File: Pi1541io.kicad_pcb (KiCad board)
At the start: 2 copper layers, 65 x 56 mm, 22 parts, among them J1 IEC1, J2 IEC2, J3 IEC3, J4 ExtSpkr, P1 Conn_02x20_Odd_Even, SW1 SW_Push, SW2 SW_Push, SW3 SW_Push, SW4 SW_Push, SW5 SW_Push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

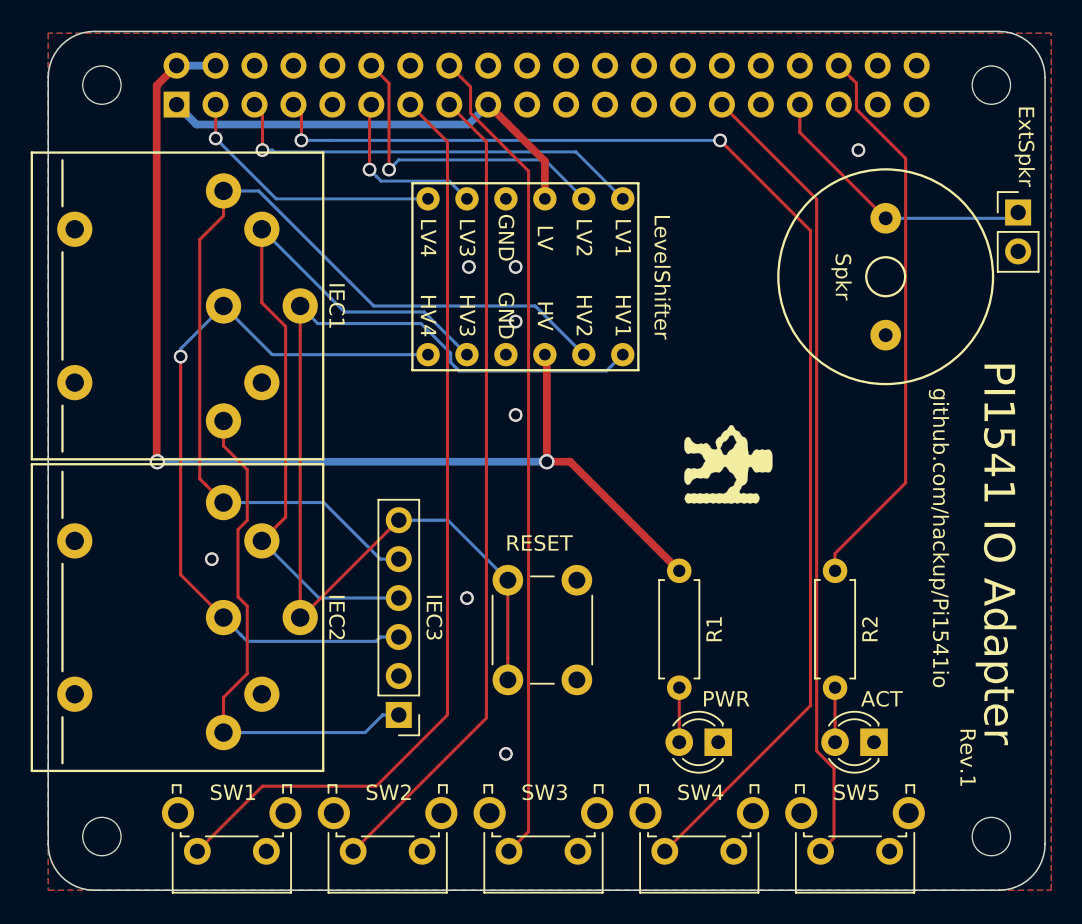
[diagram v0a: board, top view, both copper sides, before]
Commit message: Adding alternate TXS0108 level shifter module to choose from.
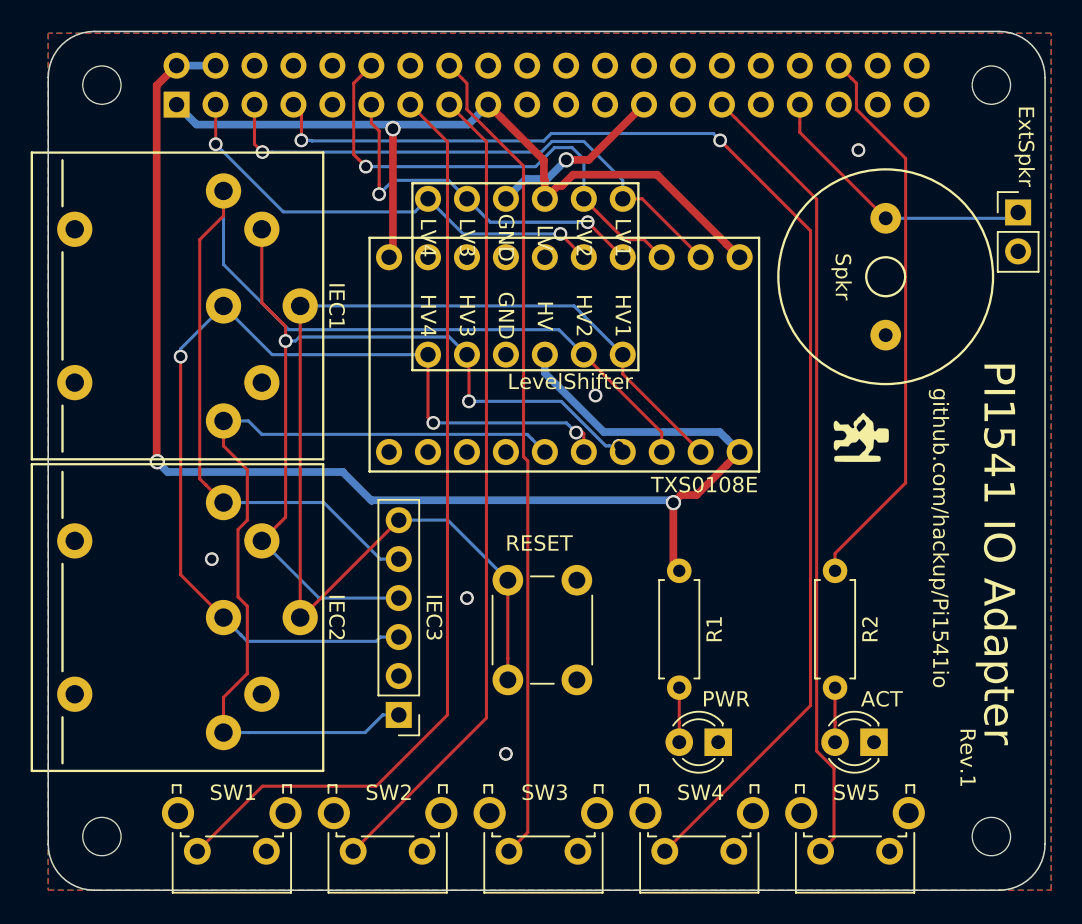
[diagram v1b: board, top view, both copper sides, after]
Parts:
- removed the G*** at (150.6, 87.5)
- added G***: LOGO, Logo:bigby2, F.Cu at (159.2, 85.7)
- added U2: TXS0108E, hackup:TXS0108Module, F.Cu at (138.5, 80.3)
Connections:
- net Net-(J1-Pad1) renamed SRQ
- J1 pad 3: Net-(J1-Pad3) -> ATN
- J1 pad 4: Net-(J1-Pad4) -> CLK
- J1 pad 5: Net-(J1-Pad5) -> DATA
- J1 pad 6: Net-(J1-Pad6) -> RESET
- J2 pad 3: Net-(J1-Pad3) -> ATN
- J2 pad 4: Net-(J1-Pad4) -> CLK
- J2 pad 5: Net-(J1-Pad5) -> DATA
- J2 pad 6: Net-(J1-Pad6) -> RESET
- J3 pad 3: Net-(J1-Pad3) -> ATN
- J3 pad 4: Net-(J1-Pad4) -> CLK
- J3 pad 5: Net-(J1-Pad5) -> DATA
- J3 pad 6: Net-(J1-Pad6) -> RESET
- P1 pad 11: CLK -> CLK_3V
- P1 pad 12: DATA -> DATA_3V
- P1 pad 3: ATN -> ATN_3V
- P1 pad 5: RESET -> RESET_3V
- SW6 pad 1: Net-(J1-Pad6) -> RESET
- U1 pad 1: RESET -> RESET_3V
- U1 pad 11: Net-(J1-Pad5) -> DATA
- U1 pad 12: Net-(J1-Pad6) -> RESET
- U1 pad 2: DATA -> DATA_3V
- U1 pad 5: CLK -> CLK_3V
- U1 pad 6: ATN -> ATN_3V
- U1 pad 7: Net-(J1-Pad3) -> ATN
- U1 pad 8: Net-(J1-Pad4) -> CLK
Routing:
- net Net-(J1-Pad6): track 68.2 -> 0.00 mm
- net Net-(J1-Pad5): track 62.5 -> 0.00 mm
- net DATA: track 21.3 -> 73.7 mm, vias 1 -> 0
- net Net-(J1-Pad3): track 49.5 -> 0.00 mm, vias 1 -> 0
- net Net-(J1-Pad4): track 48.8 -> 0.00 mm
- net CLK: track 11.4 -> 59.2 mm, vias 1 -> 3
- net ATN: track 17.7 -> 65.4 mm, vias 1 -> 3
- net RESET: track 28.0 -> 75.4 mm, vias 1 -> 0
- net RESET_3V: track 0.00 -> 36.0 mm, vias 0 -> 1
- net DATA_3V: track 0.00 -> 31.7 mm, vias 0 -> 1
- net ATN_3V: track 0.00 -> 30.4 mm, vias 0 -> 2
- net CLK_3V: track 0.00 -> 24.4 mm, vias 0 -> 2
- net +3V3: track 29.1 -> 53.4 mm, vias 0 -> 1
- net SRQ: track 34.0 -> 55.8 mm
- net +5V: track 72.9 -> 90.2 mm
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
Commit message: Reserved SRQ pin.
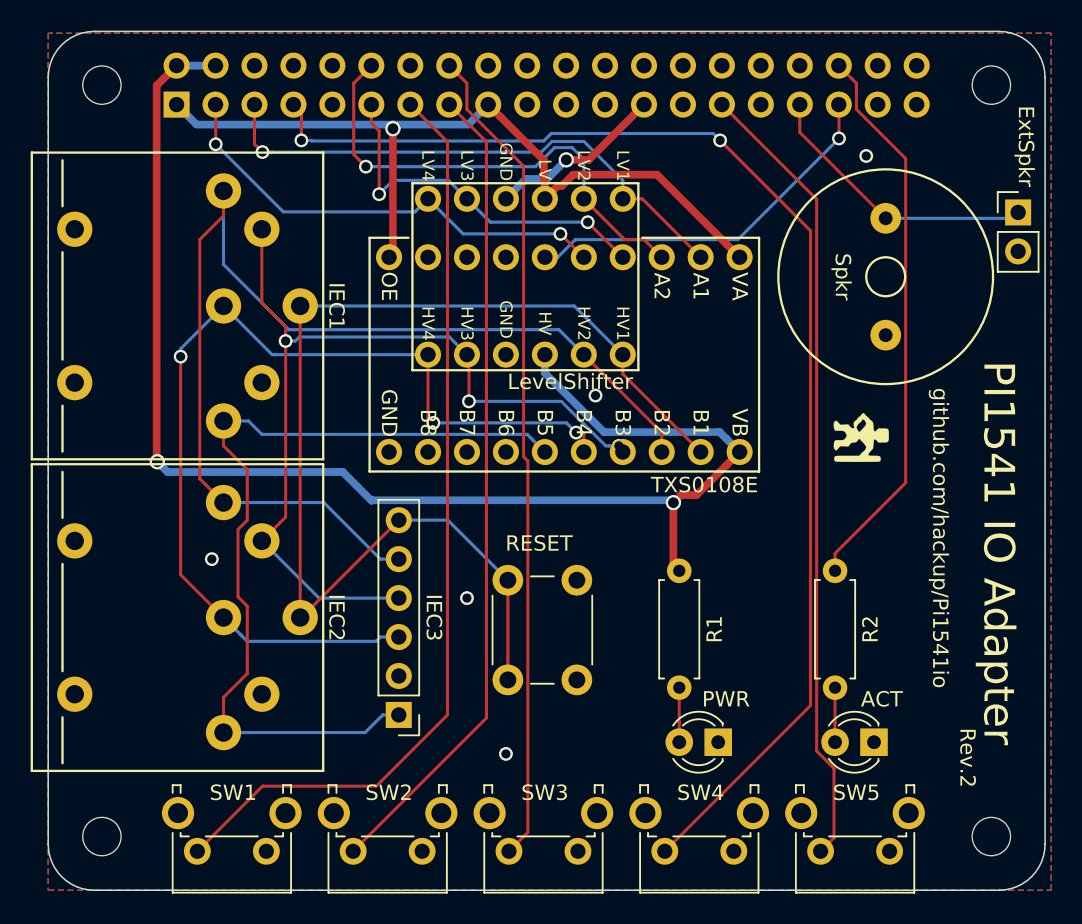
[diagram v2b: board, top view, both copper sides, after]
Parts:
- U1: footprint hackup:LevelShifterModule4CH -> LevelShifterModule4CH
- U2: footprint hackup:TXS0108Module -> TXS0108Module
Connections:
- D2 pad 1: GND -> Net-(D2-Pad1)
- P1 pad 35: /GPIO19(SPI1_MISO) -> SRQ_3V
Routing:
- net SRQ_3V: track 0.00 -> 24.6 mm, vias 0 -> 1
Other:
- board text added: "Rev.2"
- board text removed: "Rev.1"

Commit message: Fix.
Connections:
- D2 pad 1: Net-(D2-Pad1) -> GND
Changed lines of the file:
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@@
-(kicad_pcb (version 20171130) (host pcbnew "(5.0.0-rc2-dev-493-gd776eaca8)")
+(kicad_pcb (version 20171130) (host pcbnew "(5.0.0-rc2-dev-406-g05dae9627)")
   (general
     (thickness 1.6)
@@
     (zones 0)
     (modules 23)
-    (nets 40)
+    (nets 39)
   )
   (page A4)
@@
   (net 37 DATA_3V)
   (net 38 SRQ_3V)
-  (net 39 "Net-(D2-Pad1)")
   (net_class Default "This is the default net class."
     (clearance 0.2)
@@
     (add_net DATA_3V)
     (add_net "Net-(D1-Pad2)")
-    (add_net "Net-(D2-Pad1)")
     (add_net "Net-(D2-Pad2)")
     (add_net RESET)
@@
     (fp_line (start 3.7 -2.25) (end -1.15 -2.25) (layer F.CrtYd) (width 0.05))
     (pad 1 thru_hole rect (at 0 0 180) (size 1.8 1.8) (drill 0.9) (layers *.Cu *.Mask)
-      (net 39 "Net-(D2-Pad1)"))
+      (net 3 GND))
     (pad 2 thru_hole circle (at 2.54 0 180) (size 1.8 1.8) (drill 0.9) (layers *.Cu *.Mask)
       (net 32 "Net-(D2-Pad2)"))

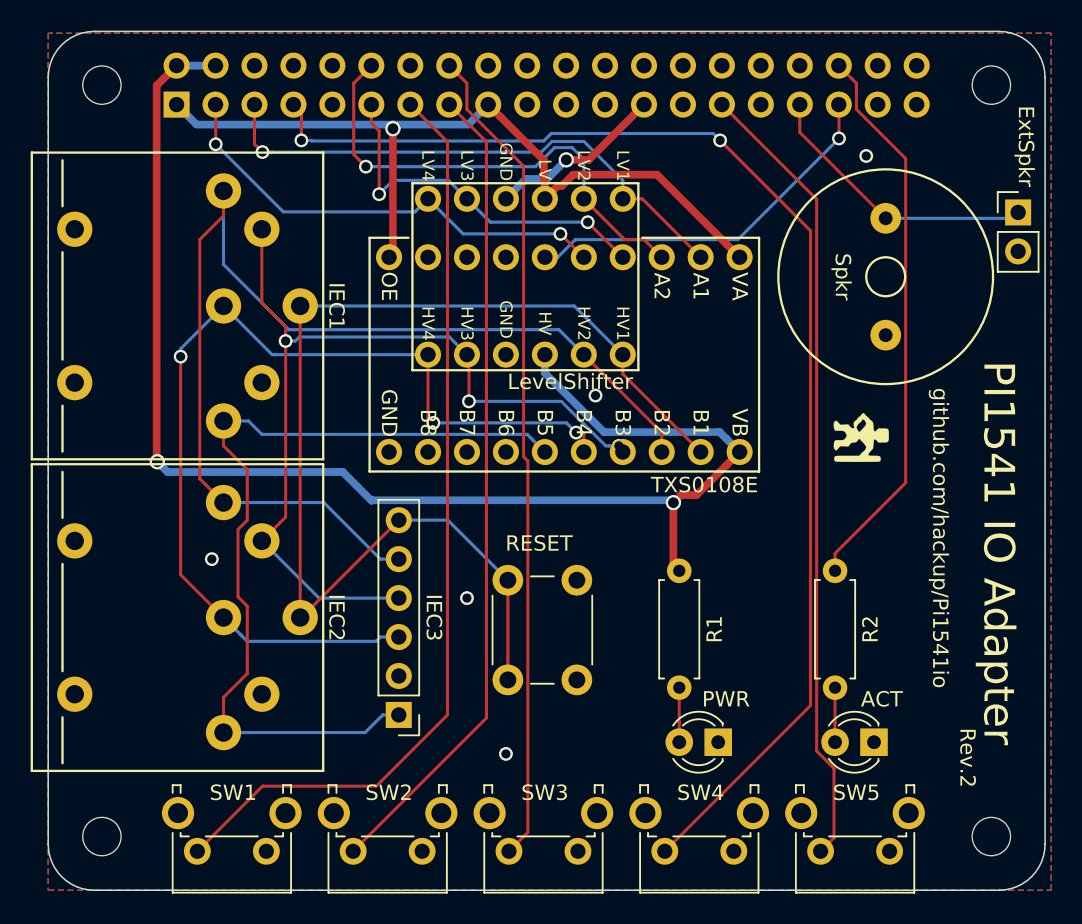
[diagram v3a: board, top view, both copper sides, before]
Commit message: Added 7406 driver for outgoing signals.
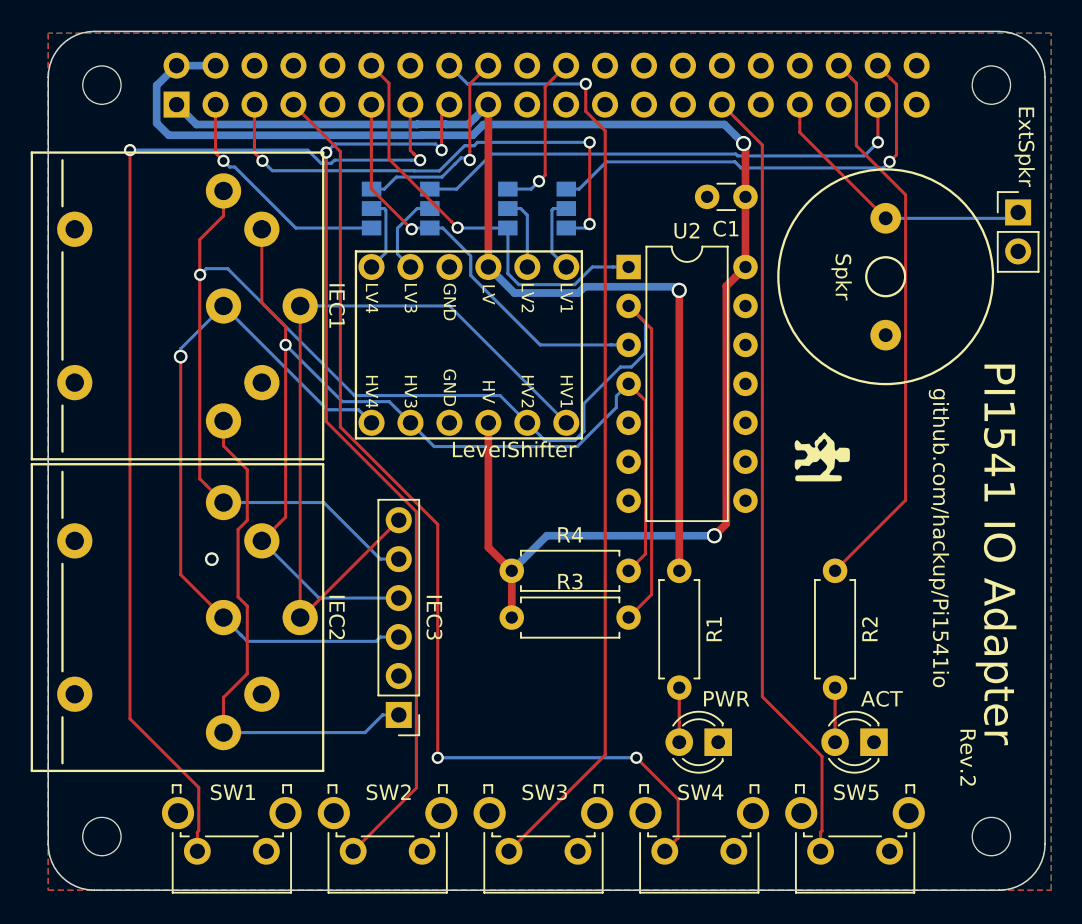
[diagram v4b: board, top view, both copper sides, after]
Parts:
- removed SW6: RESET, Buttons_Switches_THT:SW_PUSH_6mm
- added C1: C, Capacitors_THT:C_Disc_D3.0mm_W1.6mm_P2.50mm, F.Cu at (151.6, 70.0)
- added J5: GS3, Connectors:GS3, B.Cu at (139.9, 70.8)
- added J6: GS3, Connectors:GS3, B.Cu at (136.1, 70.8)
- added J7: GS3, Connectors:GS3, B.Cu at (131.0, 70.8)
- added J8: GS3, Connectors:GS3, B.Cu at (127.2, 70.8)
- added R3: 1k, Resistors_THT:R_Axial_DIN0207_L6.3mm_D2.5mm_P7.62mm_Horizontal, F.Cu at (136.4, 97.4)
- added R4: 1k, Resistors_THT:R_Axial_DIN0207_L6.3mm_D2.5mm_P7.62mm_Horizontal, F.Cu at (136.4, 94.4)
- R1: value 330 -> 220
- U1: footprint LevelShifterModule4CH -> hackup:LevelShifterModule4CH
- U2: value TXS0108E -> 7406; footprint TXS0108Module -> Housings_DIP:DIP-14_W7.62mm
- moved U2 7.90 mm to (144.0, 74.6), turned to 0 degrees
- moved U1 5.77 mm to (132.3, 79.6)
- moved G*** 2.84 mm to (156.7, 87.0)
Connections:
- P1 pad 11: CLK_3V -> CLK_BD
- P1 pad 12: DATA_3V -> DATA_BD
- P1 pad 18: /GPIO24(GEN5) -> ATN_IN
- P1 pad 22: /GPIO25(GEN6) -> DATA_IN
- P1 pad 3: ATN_3V -> ATN_BD
- P1 pad 35: SRQ_3V -> SRQ_BD
- P1 pad 37: /GPIO26 -> CLK_IN
- P1 pad 38: /GPIO20(SPI1_MOSI) -> RESET_IN
- P1 pad 5: RESET_3V -> RESET_BD
- R1 pad 1: +5V -> +3V3
- U1 pad 1: RESET_3V -> Net-(J5-Pad2)
- U1 pad 2: DATA_3V -> Net-(J6-Pad2)
- U1 pad 5: CLK_3V -> Net-(J7-Pad2)
- U1 pad 6: ATN_3V -> Net-(J8-Pad2)
- U2 pad 1: RESET_3V -> DATA_BD
- U2 pad 10: +3V3 -> (no net)
- U2 pad 11: GND -> (no net)
- U2 pad 14: (no net) -> +5V
- U2 pad 2: +3V3 -> DATA
- U2 pad 3: DATA_3V -> CLK_BD
- U2 pad 4: CLK_3V -> CLK
- U2 pad 5: ATN_3V -> (no net)
- U2 pad 6: SRQ_3V -> (no net)
- U2 pad 7: (no net) -> GND
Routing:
- net RESET_3V: track 36.0 -> 0.00 mm, vias 1 -> 0
- net RESET_BD: track 0.00 -> 33.2 mm, vias 0 -> 3
- net CLK_IN: track 0.00 -> 33.0 mm, vias 0 -> 1
- net DATA_3V: track 31.7 -> 0.00 mm, vias 1 -> 0
- net ATN_3V: track 30.4 -> 0.00 mm, vias 2 -> 0
- net RESET_IN: track 0.00 -> 29.1 mm, vias 0 -> 1
- net DATA_BD: track 0.00 -> 27.8 mm, vias 0 -> 1
- net CLK_BD: track 0.00 -> 27.3 mm, vias 0 -> 1
- net RESET: track 75.4 -> 49.9 mm
- net SRQ_3V: track 24.6 -> 0.00 mm, vias 1 -> 0
- net CLK_3V: track 24.4 -> 0.00 mm, vias 2 -> 0
- net DATA: track 73.7 -> 96.9 mm, vias 0 -> 1
- net SRQ: track 55.8 -> 34.0 mm
- net ATN: track 65.4 -> 47.6 mm, vias 3 -> 1
- net /GPIO4(GCLK): track 83.0 -> 67.0 mm, vias 3 -> 2
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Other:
- net class Default: via_dia 0.9 -> 0.8; via_drill 0.6 -> 0.5

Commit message: Silk screen corrections. Re-added reset button.
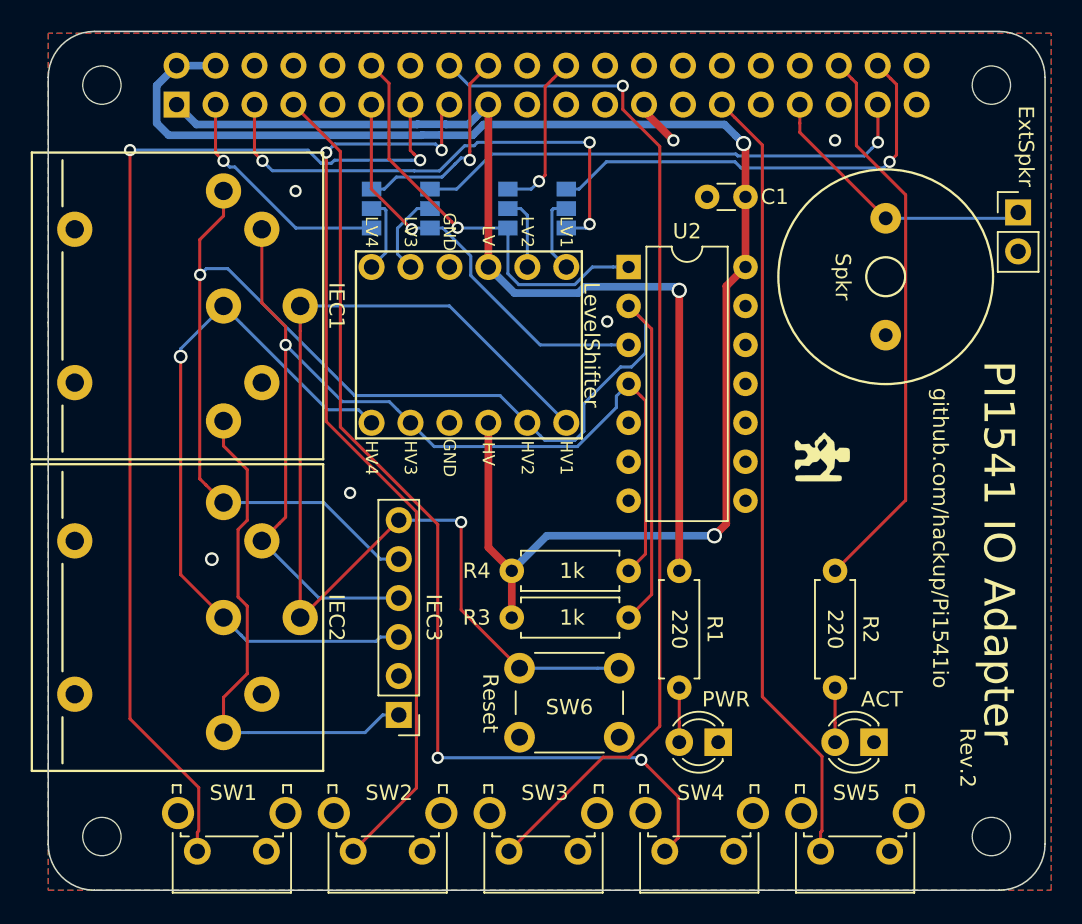
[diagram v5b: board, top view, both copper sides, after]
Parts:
- added SW6: Reset, Buttons_Switches_THT:SW_PUSH_6mm, F.Cu at (136.9, 100.7)
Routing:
- net RESET: track 49.9 -> 71.6 mm, vias 0 -> 1
- net /GPIO23(GEN4): track 62.6 -> 67.8 mm
- net GND: track 0.00 -> 3.13 mm, vias 1 -> 6
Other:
- board text added: "7406"
- board text added: "simple"
